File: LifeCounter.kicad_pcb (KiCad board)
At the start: 2 copper layers, 118 parts, among them J201 USBC, J701 Debug, Q201 2N7002, Q202 BSS84, Q801 2N7002, SW1 RotaryEncoder_Switch_MP, SW2 RotaryEncoder_Switch_MP, SW201 PWR_ON, SW701 RST, U1 74LVC3G14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

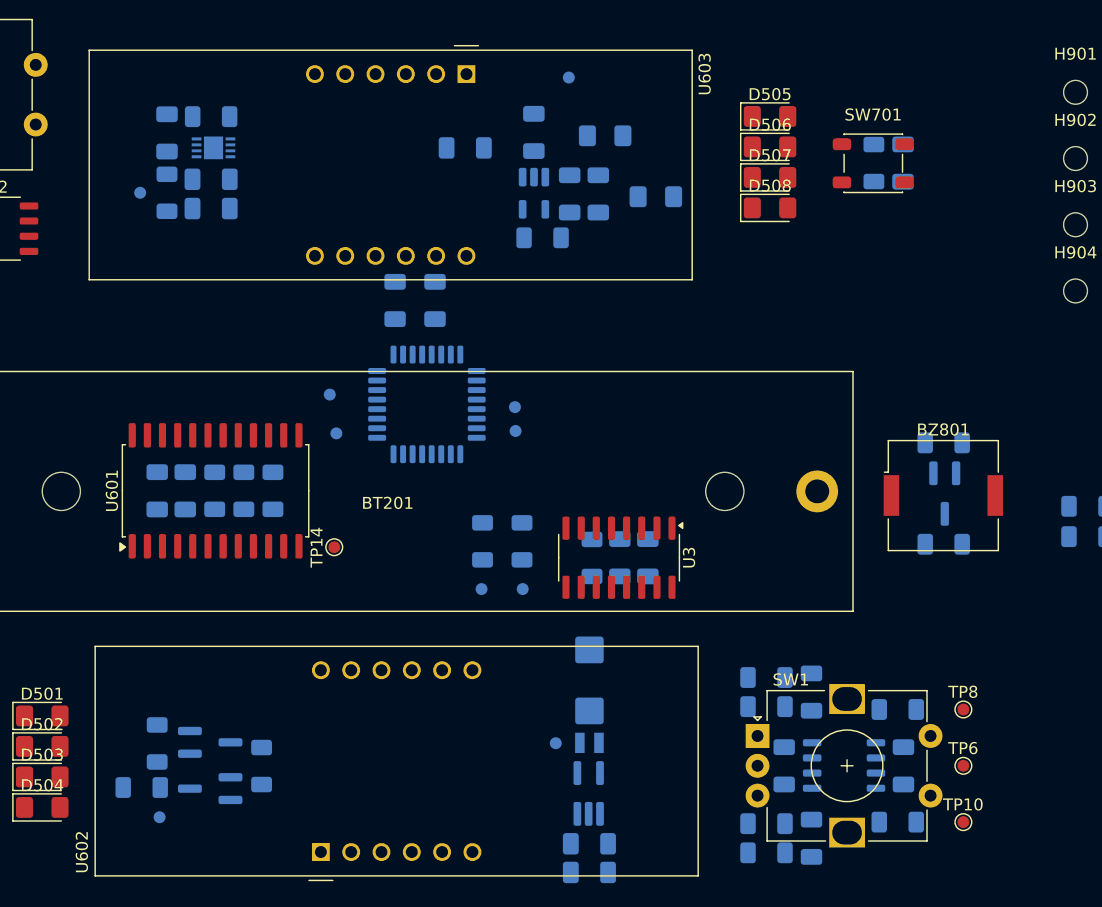
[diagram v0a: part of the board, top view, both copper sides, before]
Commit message: Organise subcircuit layouts
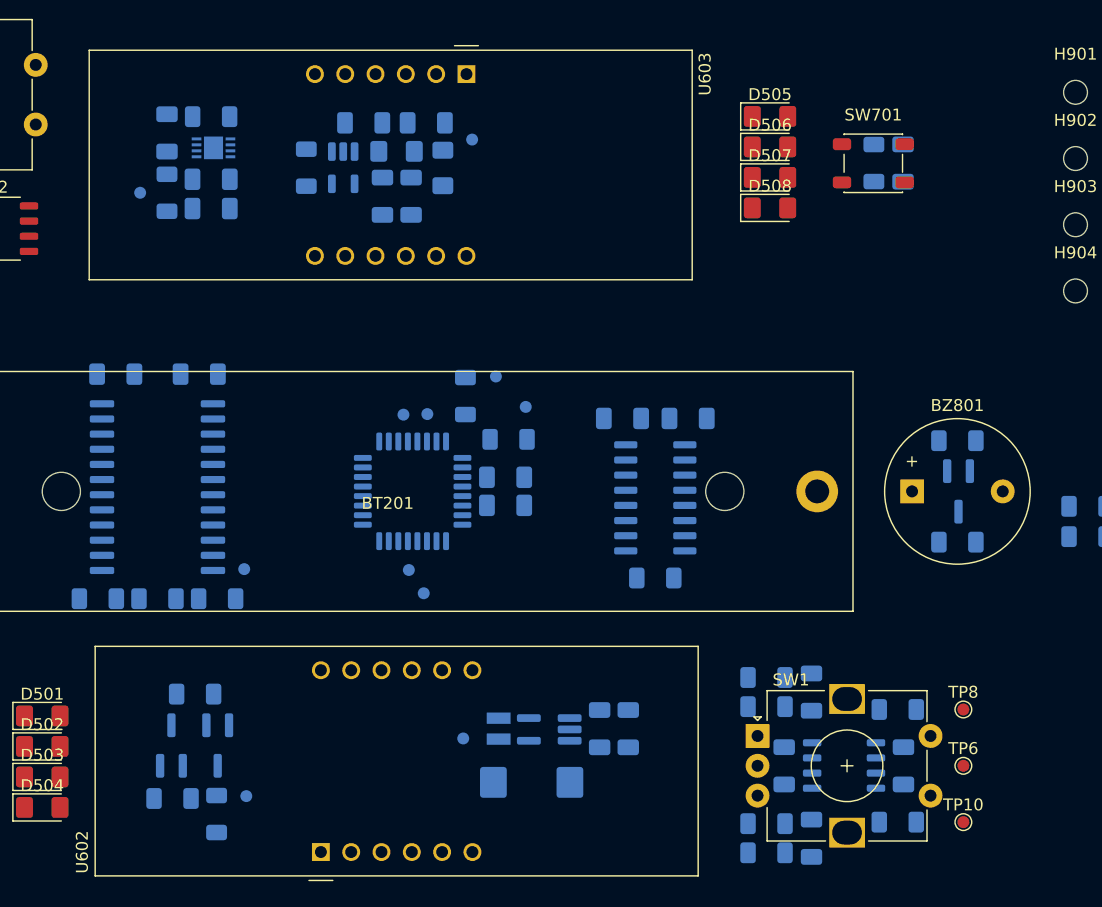
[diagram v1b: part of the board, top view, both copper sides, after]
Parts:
- BZ801: footprint Buzzer_Beeper:Buzzer_Murata_PKMCS0909E -> Buzzer_Beeper:Buzzer_12x9.5RM7.6
- C210: footprint Capacitor_Tantalum_SMD:CP_EIA-6032-28_Kemet-C_HandSolder -> Capacitor_Tantalum_SMD:CP_EIA-7343-31_Kemet-D_HandSolder
- L201: footprint Inductor_SMD_Wurth:L_Wurth_WE-LQSH-2010 -> Inductor_SMD_Wurth:L_Wurth_WE-LQSH-2512
- TP14, U3, U601: moved to B.Cu
- moved D202 22.1 mm to (-130.0, 6.50), turned to 180 degrees
- moved R205 20.7 mm to (-137.6, 7.87), turned to 90 degrees
- moved C702 18.2 mm to (-120.9, 36.2), turned to 0 degrees
- moved TP17 17.9 mm to (-121.7, 25.4), turned to 180 degrees
- moved C703 17.5 mm to (-120.9, 33.8), turned to 0 degrees
- moved R603 17.2 mm to (-155.0, 44.0), turned to 180 degrees
- moved U202 16.1 mm to (-134.5, 7.87)
- moved TP13 16.1 mm to (-129.0, 41.6), turned to 180 degrees
- moved C204 15.7 mm to (-131.2, 10.3), turned to -90 degrees
- moved C205 15.7 mm to (-128.8, 10.3), turned to -90 degrees
- moved TP12 15.3 mm to (-127.7, 43.5), turned to 180 degrees
- moved TP18 15.3 mm to (-119.2, 27.9), turned to 180 degrees
- moved D201 13.9 mm to (-126.1, 7.89), turned to -90 degrees
- moved C207 12.5 mm to (-110.6, 54.9), turned to -90 degrees
- moved R702 12.3 mm to (-124.2, 27.0)
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
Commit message: Fix encoder debounce
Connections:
- U1 pad 1: /Encoder1/B_RAW -> Net-(C3-Pad1)
- U1 pad 3: /Encoder1/A_RAW -> Net-(C2-Pad1)
- U1 pad 6: /Encoder1/BTN_RAW -> Net-(C1-Pad1)
- U2 pad 1: /Encoder2/B_RAW -> Net-(C6-Pad1)
- U2 pad 3: /Encoder2/A_RAW -> Net-(C5-Pad1)
- U2 pad 6: /Encoder2/BTN_RAW -> Net-(C4-Pad1)
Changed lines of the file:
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@@
 			(layers "F.Cu" "F.Mask" "F.Paste")
 			(roundrect_rratio 0.25)
-			(net 91 "/Encoder2/B_RAW")
+			(net 10 "Net-(C6-Pad1)")
 			(pintype "input")
 		)
@@
 			(layers "F.Cu" "F.Mask" "F.Paste")
 			(roundrect_rratio 0.25)
-			(net 90 "/Encoder2/A_RAW")
+			(net 9 "Net-(C5-Pad1)")
 			(pintype "input")
 		)
@@
 			(layers "F.Cu" "F.Mask" "F.Paste")
 			(roundrect_rratio 0.25)
-			(net 89 "/Encoder2/BTN_RAW")
+			(net 8 "Net-(C4-Pad1)")
 			(pintype "input")
 		)
@@
 			(layers "B.Cu" "B.Mask" "B.Paste")
 			(roundrect_rratio 0.25)
-			(net 88 "/Encoder1/B_RAW")
+			(net 7 "Net-(C3-Pad1)")
 			(pintype "input")
 		)
@@
 			(layers "B.Cu" "B.Mask" "B.Paste")
 			(roundrect_rratio 0.25)
-			(net 87 "/Encoder1/A_RAW")
+			(net 6 "Net-(C2-Pad1)")
 			(pintype "input")
 		)
@@
 			(layers "B.Cu" "B.Mask" "B.Paste")
 			(roundrect_rratio 0.25)
-			(net 86 "/Encoder1/BTN_RAW")
+			(net 5 "Net-(C1-Pad1)")
 			(pintype "input")
 		)

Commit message: Initial board layout
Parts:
- C4, C5, C6, C8, R10, R11, R12, R201, R202, R211, R212, R7, R8, R9, TP1, U2: moved to B.Cu
- moved H903 193.6 mm to (71.7, 141.2)
- moved R7 191.0 mm to (-6.97, 76.8)
- moved R10 190.7 mm to (-6.97, 86.3)
- moved R211 184.5 mm to (-19.2, 105.0), turned to 90 degrees
- moved R4 184.0 mm to (61.4, 140.8)
- moved R9 182.4 mm to (-18.0, 86.4), turned to 180 degrees
- moved TP7 181.9 mm to (-1.47, 81.6)
- moved R3 181.7 mm to (61.4, 138.4), turned to 0 degrees
- moved TP11 181.4 mm to (-1.47, 86.3)
- moved SW1 180.8 mm to (62.1, 135.9), turned to 180 degrees
- moved C702 180.0 mm to (43.6, 109.5)
- moved C703 180.0 mm to (43.6, 107.2)
- moved R701 180.0 mm to (43.8, 104.0)
- moved R702 180.0 mm to (40.2, 100.3)
- moved TP12 180.0 mm to (36.7, 116.9)
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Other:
- board outline added: 103 x 73 mm

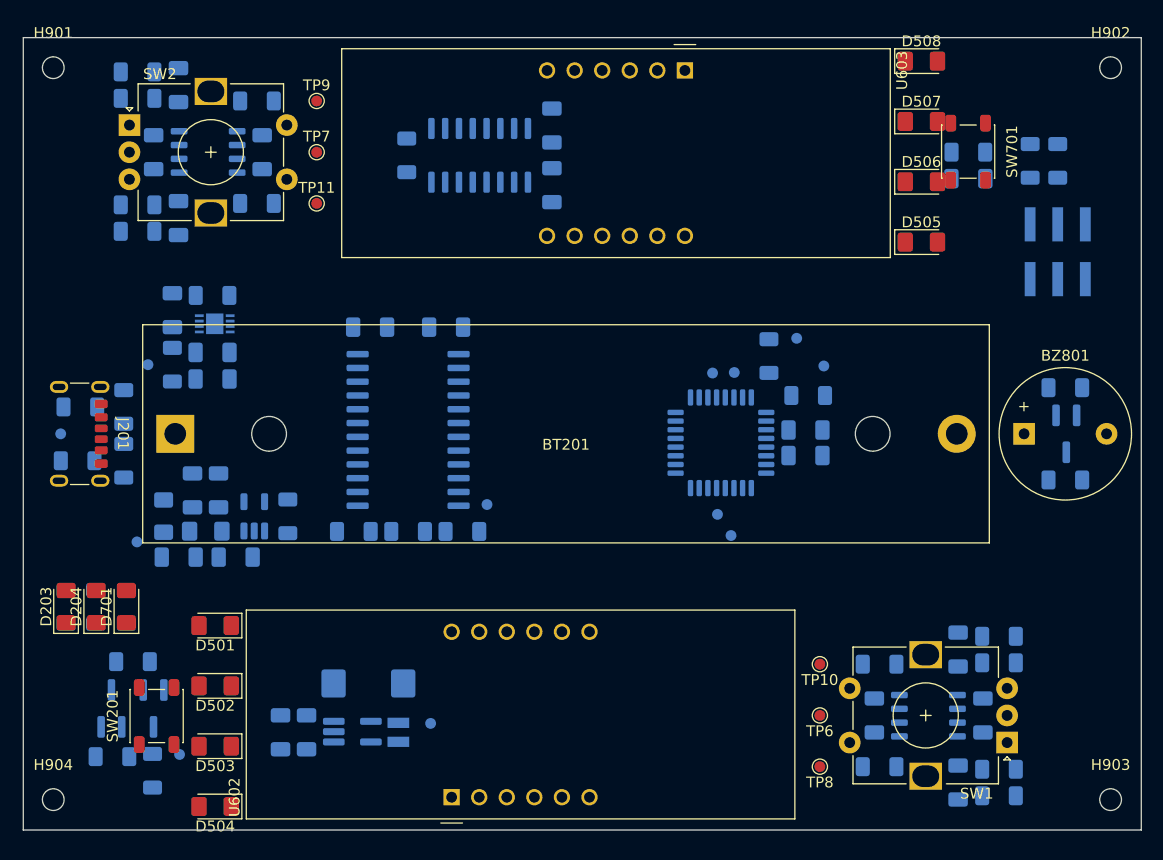
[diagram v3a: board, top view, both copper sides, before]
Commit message: Started routing component blocks
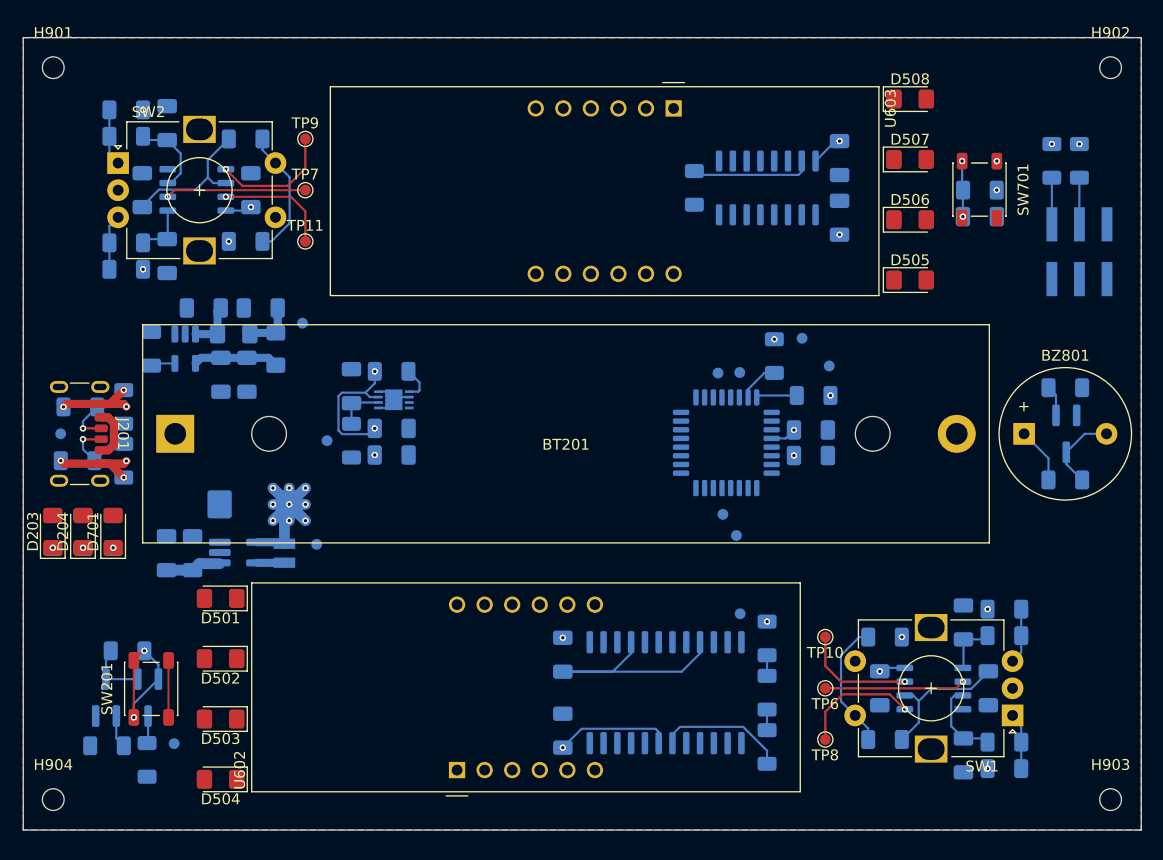
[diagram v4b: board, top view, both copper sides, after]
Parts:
- moved R603 42.9 mm to (40.0, 136.3), turned to -90 degrees
- moved C602 41.2 mm to (21.2, 134.8), turned to 90 degrees
- moved R602 36.3 mm to (40.0, 131.3), turned to -90 degrees
- moved U601 33.9 mm to (30.7, 131.3), turned to -90 degrees
- moved C601 32.0 mm to (21.2, 127.8), turned to -90 degrees
- moved R601 29.8 mm to (40.0, 126.3), turned to 90 degrees
- moved C501 26.7 mm to (46.7, 87.6)
- moved C502 26.7 mm to (46.7, 82.1)
- moved R501 26.7 mm to (33.3, 84.8)
- moved U3 26.7 mm to (40.0, 84.8)
- moved TP14 25.4 mm to (37.5, 124.1), turned to 90 degrees
- moved TP2 25.3 mm to (-2.78, 97.3), turned to 0 degrees
- moved C209 24.2 mm to (-6.62, 95.9), turned to 180 degrees
- moved C206 23.1 mm to (-11.9, 95.9), turned to 180 degrees
- moved R205 19.9 mm to (-16.7, 99.7), turned to 90 degrees
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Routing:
- net VCC: track 0.00 -> 60.1 mm, vias 0 -> 32
- net GND: track 0.00 -> 44.9 mm, vias 0 -> 7
- net /Power/VIN: track 0.00 -> 24.2 mm, vias 0 -> 2
- net Net-(C4-Pad1): track 0.00 -> 13.4 mm
- net Net-(C1-Pad1): track 0.00 -> 13.2 mm
- net /Controller/Encoder2.BTN: track 0.00 -> 12.9 mm, vias 0 -> 1
- net /Controller/Encoder1.BTN: track 0.00 -> 12.9 mm, vias 0 -> 1
- net VBUS: track 0.00 -> 12.7 mm
- net /Encoder2/BTN_RAW: track 0.00 -> 12.0 mm
- net /Encoder1/BTN_RAW: track 0.00 -> 12.0 mm
- net Net-(U601-ISET): track 0.00 -> 11.9 mm
- net /Controller/Encoder2.CLK: track 0.00 -> 11.3 mm, vias 0 -> 1
- net Net-(U3-R-EXT): track 0.00 -> 11.1 mm
- net /Controller/Encoder1.CLK: track 0.00 -> 11.1 mm, vias 0 -> 1
- net /Controller/Encoder2.DAT: track 0.00 -> 10.7 mm, vias 0 -> 1
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- added copper zone on B.Cu, net GND
- added copper zone on F.Cu, net VCC

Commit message: Routing player status LEDs and display
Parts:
- moved C201 3.96 mm to (1.68, 108.2)
- moved C202 3.96 mm to (1.68, 105.8)
- moved R203 3.96 mm to (-2.02, 106.9)
- moved TP3 3.96 mm to (-4.27, 106.9)
- moved C203 3.96 mm to (-2.02, 101.9)
- moved R204 3.96 mm to (1.68, 100.5)
- moved U201 3.96 mm to (1.88, 103.1)
- moved TP14 1.14 mm to (38.5, 123.5)
- moved C601 1.05 mm to (22.2, 127.5)
- moved C602 1.05 mm to (22.2, 134.5)
- moved R601 1.05 mm to (41.0, 126.0)
- moved R602 1.05 mm to (41.0, 131.0)
- moved R603 1.05 mm to (41.0, 136.0)
- moved U601 1.05 mm to (31.7, 131.0)
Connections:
- U701 pad 15: /Controller/Encoder2.A -> /Controller/Encoder2.CLK
- U701 pad 16: /Controller/Encoder2.B -> /Controller/Encoder2.DAT
- U701 pad 7: /Controller/Encoder1.A -> /Controller/Encoder1.CLK
- U701 pad 8: /Controller/Encoder1.B -> /Controller/Encoder1.DAT
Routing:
- net /Display/E: track 0.00 -> 104.2 mm, vias 0 -> 2
- net /Display/Digit2_4: track 0.00 -> 102.3 mm, vias 0 -> 1
- net /Display/D: track 0.00 -> 101.3 mm, vias 0 -> 2
- net /Display/G: track 0.00 -> 99.9 mm, vias 0 -> 2
- net /Display/A: track 0.00 -> 99.3 mm, vias 0 -> 3
- net /Display/C: track 0.00 -> 97.9 mm, vias 0 -> 2
- net /Display/DP: track 0.00 -> 96.6 mm, vias 0 -> 2
- net /Display/F: track 0.00 -> 91.6 mm, vias 0 -> 3
- net Net-(D504-K): track 0.00 -> 90.1 mm, vias 0 -> 1
- net Net-(D503-K): track 0.00 -> 86.5 mm, vias 0 -> 1
- net Net-(D502-K): track 0.00 -> 82.7 mm, vias 0 -> 1
- net /Display/Digit2_1: track 0.00 -> 82.6 mm, vias 0 -> 1
- net /Display/B: track 0.00 -> 82.2 mm, vias 0 -> 1
- net Net-(D501-K): track 0.00 -> 82.0 mm, vias 0 -> 1
- net /Display/Digit2_2: track 0.00 -> 80.2 mm, vias 0 -> 1
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
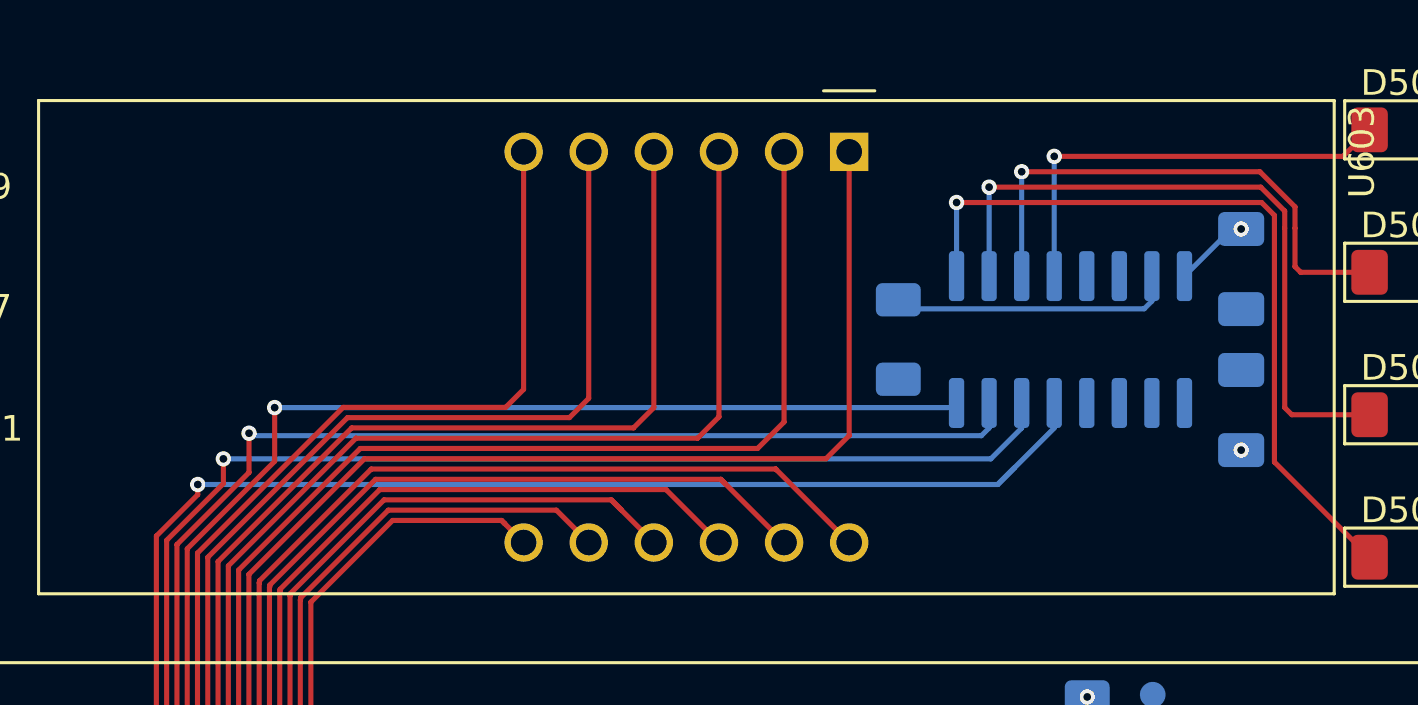
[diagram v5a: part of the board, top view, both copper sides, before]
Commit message: Center led driver
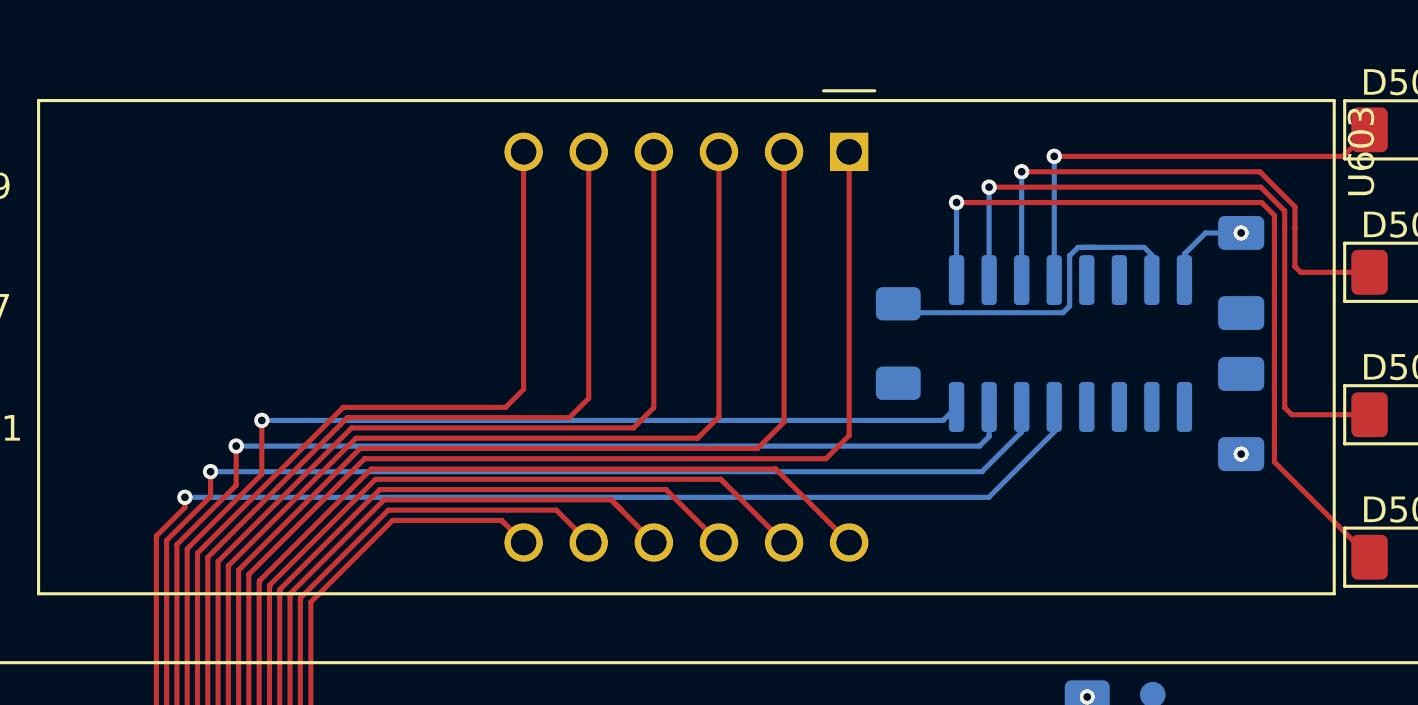
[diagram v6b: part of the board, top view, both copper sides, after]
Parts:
- moved C501 0.15 mm to (46.7, 87.7)
- moved C502 0.15 mm to (46.7, 82.2)
- moved R501 0.15 mm to (33.3, 85.0)
- moved U3 0.15 mm to (40.0, 85.0)
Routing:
- net Net-(U3-R-EXT): track 11.1 -> 15.3 mm
- net Net-(D501-K): track 82.0 -> 81.0 mm
- net VCC: track 71.3 -> 71.9 mm
